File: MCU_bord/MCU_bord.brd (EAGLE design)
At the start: 100 x 80 mm, 1 part

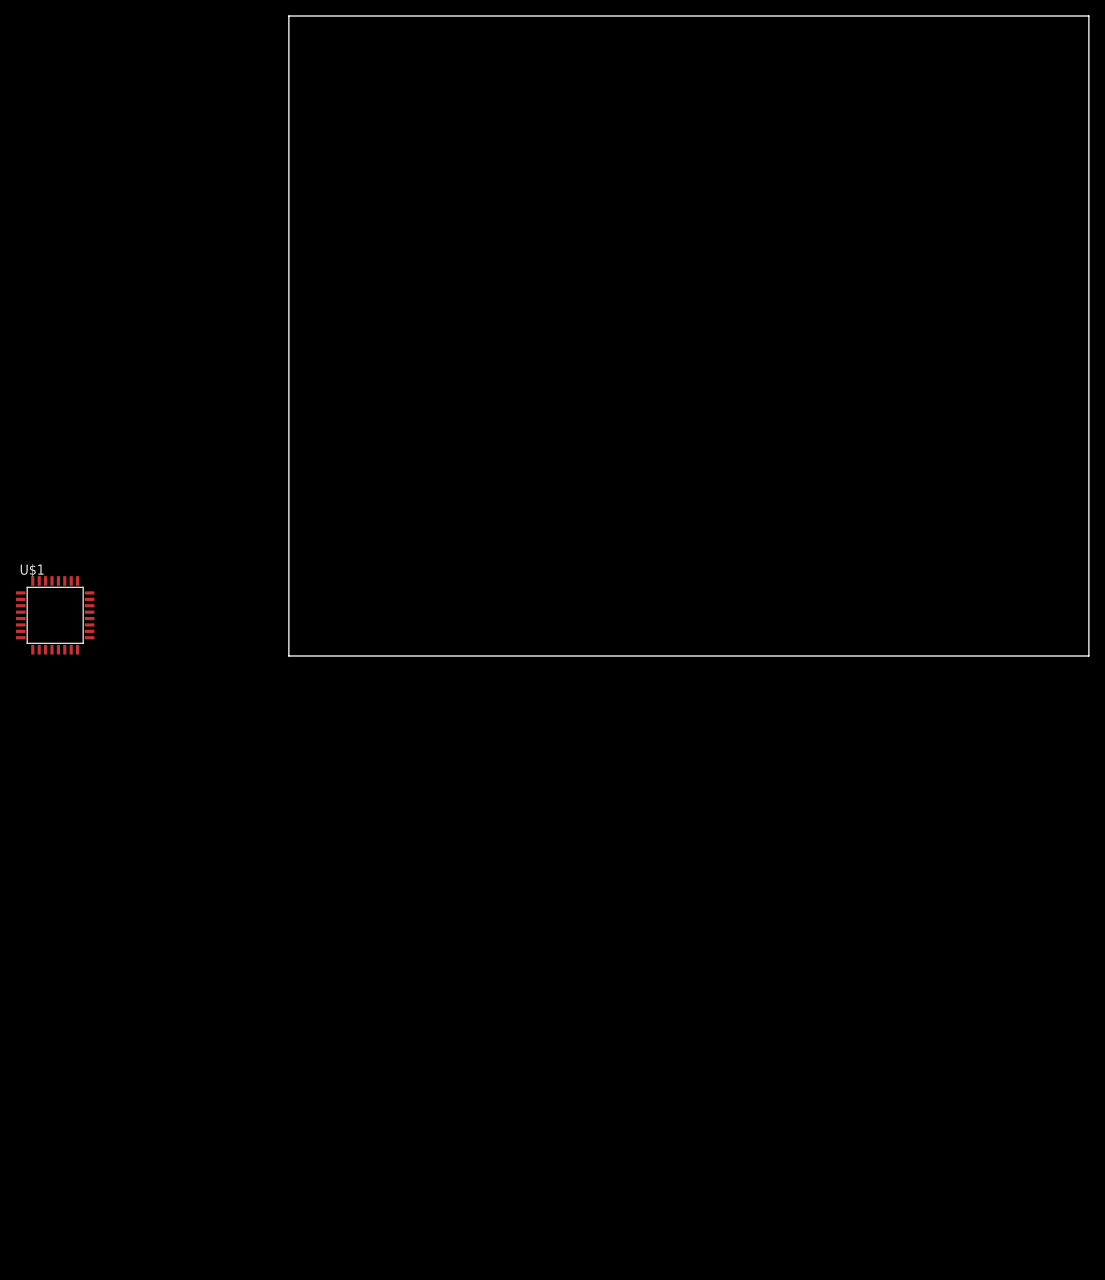
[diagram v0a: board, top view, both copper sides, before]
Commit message: mcu側に着手
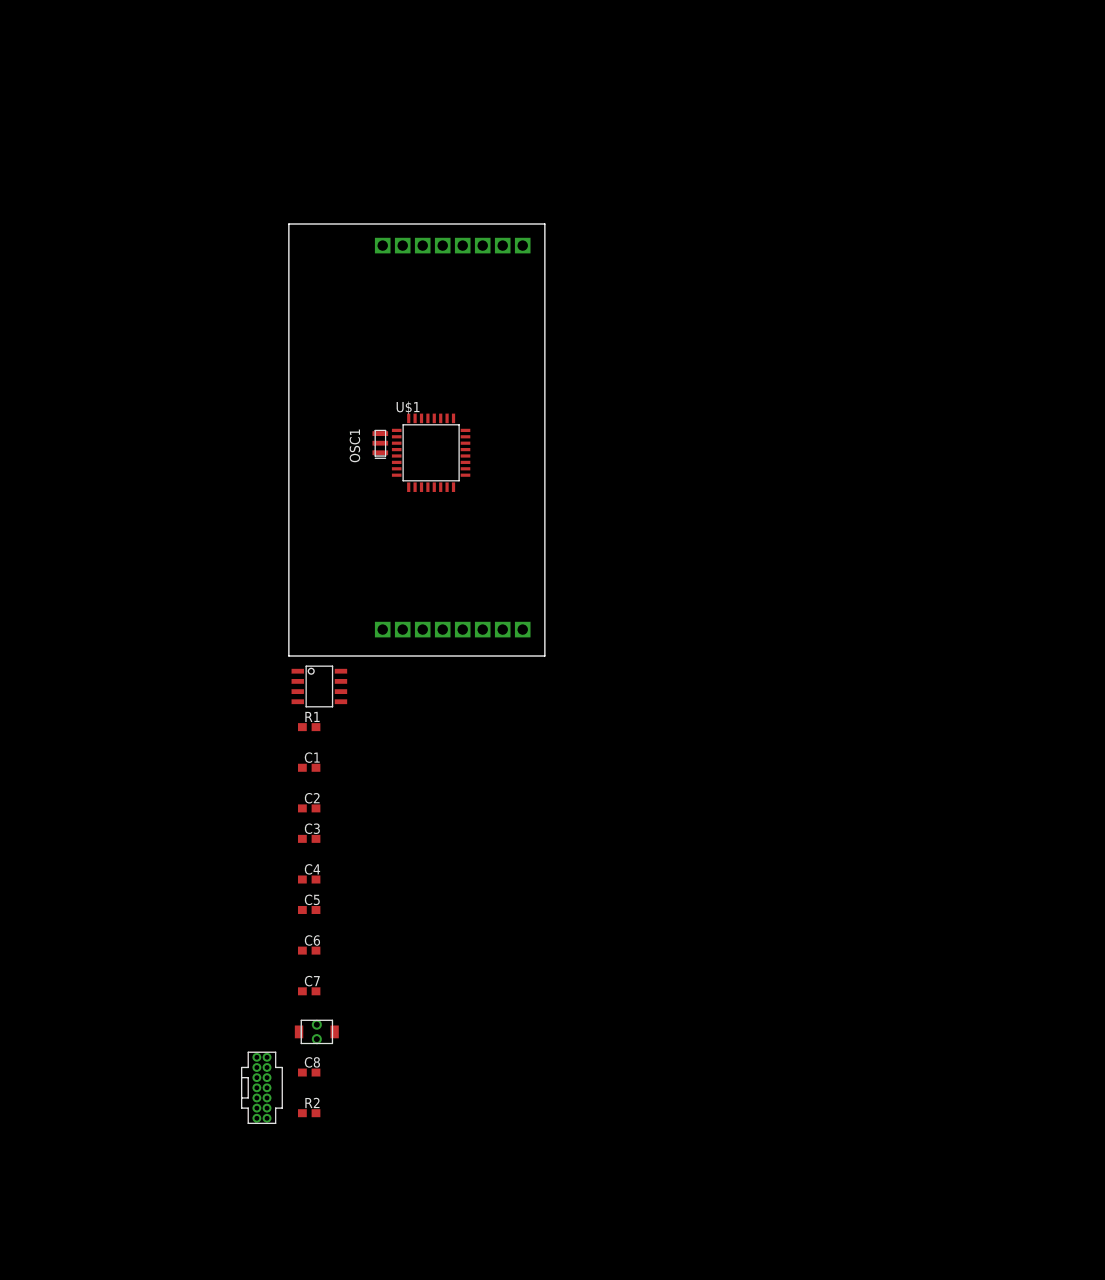
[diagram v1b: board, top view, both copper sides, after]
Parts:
- added C1, C4, C8: 0.1u, rcl:C1608
- added C2, C3, C7: 10u, rcl:C1608
- added C5: 4.7u, rcl:C1608
- added C6: 1u, rcl:C1608
- added CON1, CON2: (no value), user_conector:JQ_S8P
- added IC1: (no value), user_ic:SOIC8
- added OSC1: 12M, user_osc:CSTNE#
- added R1, R2: 10k, user_rcl:1608
- added U$2: TAKUTOSUITTI2, user_swich:TAKUTOSUITTI2
- added U$3: BOX14P, user_conector:CON_HEDA14P_1.27
- moved U$1 51.2 mm to (17.8, 25.4)
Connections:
- new net +3V3: C2.1, C4.2, C5.1, CON1.P$6, IC1.P$5, U$1.1, U$1.17
- new net +5V: C1.1, C3.1, CON1.P$5, IC1.P$3, R1.1
- new net CAN_N: CON2.P$8, IC1.P$6
- new net CAN_P: CON2.P$7, IC1.P$7
- new net CAN_RX: IC1.P$4, U$1.21
- new net CAN_TX: IC1.P$1, U$1.22
- new net COAST: CON1.P$3
- new net DIR: CON1.P$4
- new net FF1: CON1.P$2
- new net FF2: CON1.P$1
- new net GND: C1.2, C2.2, C3.2, C4.1, C5.2, C6.2, C7.2, C8.2, CON1.P$7, CON1.P$8, CON2.P$1, CON2.P$3, IC1.P$2, OSC1.P$2, R2.2, U$1.16, U$1.32, U$2.P$1, U$3.11, U$3.5, U$3.7
- new net N$1: OSC1.P$1, U$1.3
- new net N$2: OSC1.P$3, U$1.2
- new net N$3: R2.1, U$1.31
- new net N$7: IC1.P$8, R1.2
- new net NRST: U$1.4, U$3.12
- new net PWM: CON2.P$5
- new net RESET: CON2.P$6
- new net T_JCLK/SWCLK: U$1.24, U$3.6
- new net T_JTDI: U$1.25, U$3.10
- new net T_JTDO/SWO: U$1.26, U$3.8
- new net T_JTMS/SWDIO: U$1.23, U$3.4
- new net T_VCC: U$3.3
- new net T_VCP_RX: U$1.30, U$3.13
- new net T_VCP_TX: U$1.29, U$3.14
- new net VDDA: C6.1, C7.1, C8.1, CON2.P$4, U$1.5, U$2.P$2
- new net VIOUT: CON2.P$2
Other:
- board size 100 x 80 mm -> 32 x 54 mm

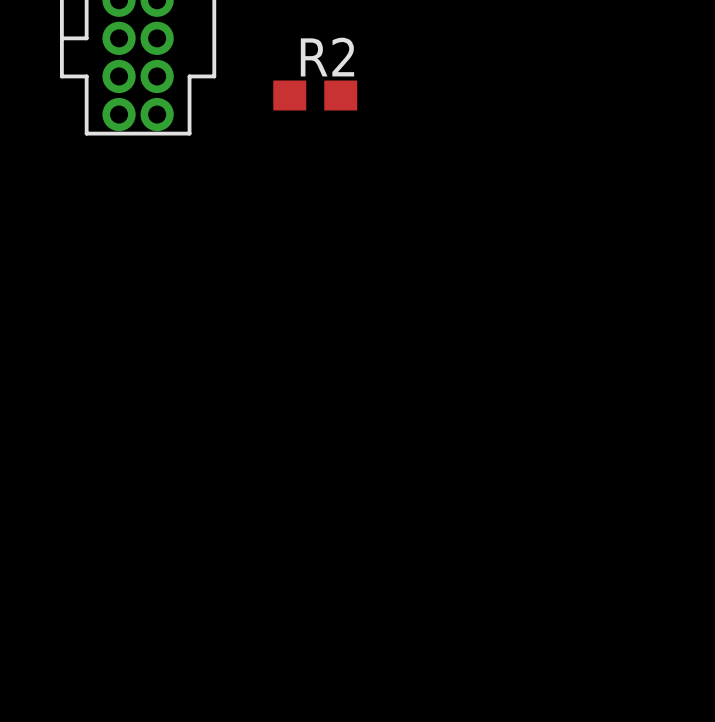
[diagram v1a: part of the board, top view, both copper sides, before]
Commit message: mcu側回路図多分完成。基板側に着手する予定
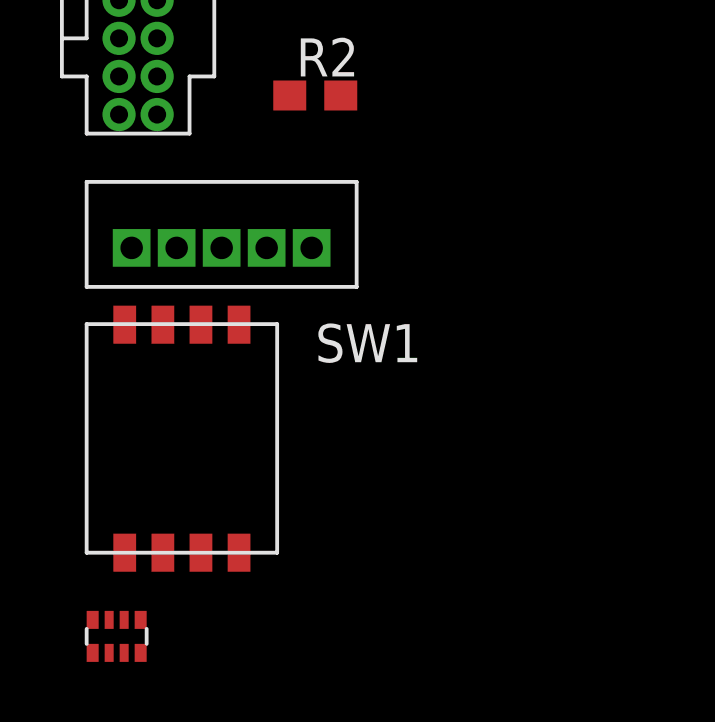
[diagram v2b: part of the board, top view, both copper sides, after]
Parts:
- added R_I1: (no value), user_rcl:1005X4RESISTOR
- added SW1: (no value), user_swich:DIPSW4
- added U$4: ZH_5P, user_conector:ZH_5P
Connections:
- new net A_CH: U$1.20, U$4.PIN3
- new net B_CH: U$1.19, U$4.PIN1
- new net ID1: R_I1.1, SW1.P$8, U$1.15
- new net ID2: R_I1.2, SW1.P$7, U$1.18
- new net ID3: R_I1.3, SW1.P$6, U$1.27
- new net ID4: R_I1.4, SW1.P$5, U$1.28
- net +3V3: now also R_I1.5, R_I1.6, R_I1.7, R_I1.8
- net +5V: now also U$4.PIN2
- net COAST: now also U$1.7
- net DIR: now also U$1.6
- net FF1: now also U$1.8
- net FF2: now also U$1.9
- net GND: now also SW1.P$1, SW1.P$2, SW1.P$3, SW1.P$4, U$4.PIN5
- net PWM: now also U$1.14
- net RESET: now also U$1.13
- net VIOUT: now also U$1.11
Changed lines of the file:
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@@
 </element>
 <element name="U$3" library="user_conector" package="CON_HEDA14P_1.27" value="BOX14P" x="-5.08" y="-58.42" smashed="yes"/>
+<element name="U$4" library="user_conector" package="ZH_5P" value="ZH_5P" x="-5.08" y="-62.23" smashed="yes"/>
+<element name="SW1" library="user_swich" package="DIPSW4" value="" x="-2.54" y="-68.58" smashed="yes">
+<attribute name="NAME" x="2.54" y="-66.04" size="1.27" layer="25"/>
+<attribute name="VALUE" x="2.54" y="-71.12" size="1.27" layer="27"/>
+</element>
+<element name="R_I1" library="user_rcl" package="1005X4RESISTOR" value="" x="-5.08" y="-74.93" smashed="yes"/>
 </elements>
 <signals>
@@
 <signal name="FF2">
 <contactref element="CON1" pad="P$1"/>
+<contactref element="U$1" pad="9"/>
+<wire x1="14.98" y1="21.1" x2="11.73" y2="51.3" width="0" layer="19" extent="1-1"/>
 </signal>
 <signal name="FF1">
 <contactref element="CON1" pad="P$2"/>
+<contactref element="U$1" pad="8"/>
+<wire x1="13.48" y1="22.6" x2="14.23" y2="51.3" width="0" layer="19" extent="1-1"/>
 </signal>
 <signal name="COAST">
 <contactref element="CON1" pad="P$3"/>
+<contactref element="U$1" pad="7"/>
+<wire x1="13.48" y1="23.4" x2="16.73" y2="51.3" width="0" layer="19" extent="1-1"/>
 </signal>
 <signal name="DIR">
 <contactref element="CON1" pad="P$4"/>
+<contactref element="U$1" pad="6"/>
+<wire x1="13.48" y1="24.2" x2="19.23" y2="51.3" width="0" layer="19" extent="1-1"/>
 </signal>
 <signal name="VIOUT">
 <contactref element="CON2" pad="P$2"/>
+<contactref element="U$1" pad="11"/>
+<wire x1="14.23" y1="3.3" x2="16.58" y2="21.1" width="0" layer="19" extent="1-1"/>
 </signal>
 <signal name="VDDA">
@@
 <signal name="PWM">
 <contactref element="CON2" pad="P$5"/>
+<contactref element="U$1" pad="14"/>
+<wire x1="21.73" y1="3.3" x2="18.98" y2="21.1" width="0" layer="19" extent="1-1"/>
 </signal>
 <signal name="RESET">
 <contactref element="CON2" pad="P$6"/>
+<contactref element="U$1" pad="13"/>
+<wire x1="24.23" y1="3.3" x2="18.18" y2="21.1" width="0" layer="19" extent="1-1"/>
 </signal>
 <signal name="CAN_P">
@@
 <contactref element="U$3" pad="7"/>
 <contactref element="U$3" pad="5"/>
+<contactref element="U$4" pad="PIN5"/>
+<contactref element="SW1" pad="P$1"/>
+<contactref element="SW1" pad="P$4"/>
+<contactref element="SW1" pad="P$3"/>
+<contactref element="SW1" pad="P$2"/>
 <wire x1="26.73" y1="51.3" x2="29.23" y2="51.3" width="0" layer="19" extent="1-1"/>
 <wire x1="14.98" y1="29.7" x2="26.73" y2="51.3" width="0" layer="19" extent="1-1"/>
@@
 <wire x1="3.39" y1="-52.07" x2="1.27" y2="-46.99" width="0" layer="19" extent="1-1"/>
 <wire x1="3.39" y1="-57.15" x2="3.39" y2="-52.07" width="0" layer="19" extent="1-1"/>
+<wire x1="2.42" y1="-62.23" x2="3.39" y2="-57.15" width="0" layer="19" extent="1-1"/>
 <wire x1="-4" y1="-56.515" x2="3.39" y2="-57.15" width="0" layer="19" extent="1-1"/>
 <wire x1="-4" y1="-53.975" x2="-4" y2="-56.515" width="0" layer="19" extent="1-1"/>
 <wire x1="-4" y1="-52.705" x2="-4" y2="-53.975" width="0" layer="19" extent="1-1"/>
+<wire x1="0" y1="-72.39" x2="2.42" y2="-62.23" width="0" layer="19" extent="1-1"/>
+<wire x1="-1.27" y1="-72.39" x2="0" y2="-72.39" width="0" layer="19" extent="1-1"/>
+<wire x1="-2.54" y1="-72.39" x2="-1.27" y2="-72.39" width="0" layer="19" extent="1-1"/>
+<wire x1="-3.81" y1="-72.39" x2="-2.54" y2="-72.39" width="0" layer="19" extent="1-1"/>
 </signal>
 <signal name="+5V">
@@
 <contactref element="C1" pad="1"/>
 <contactref element="C3" pad="1"/>
+<contactref element="U$4" pad="PIN2"/>
 <wire x1="1.11" y1="-4.445" x2="21.73" y2="51.3" width="0" layer="19" extent="1-1"/>
 <wire x1="1.69" y1="-8.89" x2="1.11" y2="-4.445" width="0" layer="19" extent="1-1"/>
 <wire x1="1.69" y1="-13.97" x2="1.69" y2="-8.89" width="0" layer="19" extent="1-1"/>
 <wire x1="1.69" y1="-22.86" x2="1.69" y2="-13.97" width="0" layer="19" extent="1-1"/>
+<wire x1="-2.08" y1="-62.23" x2="1.69" y2="-22.86" width="0" layer="19" extent="1-1"/>
 </signal>
 <signal name="+3V3">
@@
 <contactref element="C4" pad="2"/>
 <contactref element="C5" pad="1"/>
-<wire x1="13.48" y1="28.2" x2="24.23" y2="51.3" width="0" layer="19" extent="1-1"/>
-<wire x1="22.08" y1="22.6" x2="13.48" y2="28.2" width="0" layer="19" extent="1-1"/>
-<wire x1="6.51" y1="-5.715" x2="22.08" y2="22.6" width="0" layer="19" extent="1-1"/>
-<wire x1="1.69" y1="-19.05" x2="6.51" y2="-5.715" width="0" layer="19" extent="1-1"/>
-<wire x1="3.39" y1="-27.94" x2="1.69" y2="-19.05" width="0" layer="19" extent="1-1"/>
-<wire x1="1.69" y1="-31.75" x2="3.39" y2="-27.94" width="0" layer="19" extent="1-1"/>
+<contactref element="R_I1" pad="8"/>
+<contactref element="R_I1" pad="5"/>
+<contactref element="R_I1" pad="7"/>
+<contactref element="R_I1" pad="6"/>
+<wire x1="-4.33" y1="-74.63" x2="-4.88" y2="-74.63" width="0" layer="19" extent="1-1"/>
+<wire x1="-3.83" y1="-74.63" x2="-4.33" y2="-74.63" width="0" layer="19" extent="1-1"/>
+<wire x1="-3.28" y1="-74.63" x2="-3.83" y2="-74.63" width="0" layer="19" extent="1-1"/>
+<wire x1="1.69" y1="-31.75" x2="-3.28" y2="-74.63" width="0" layer="19" extent="1-1"/>
+<wire x1="3.39" y1="-27.94" x2="1.69" y2="-31.75" width="0" layer="19" extent="1-1"/>
+<wire x1="1.69" y1="-19.05" x2="3.39" y2="-27.94" width="0" layer="19" extent="1-1"/>
+<wire x1="6.51" y1="-5.715" x2="1.69" y2="-19.05" width="0" layer="19" extent="1-1"/>
+<wire x1="22.08" y1="22.6" x2="6.51" y2="-5.715" width="0" layer="19" extent="1-1"/>
+<wire x1="13.48" y1="28.2" x2="22.08" y2="22.6" width="0" layer="19" extent="1-1"/>
+<wire x1="24.23" y1="51.3" x2="13.48" y2="28.2" width="0" layer="19" extent="1-1"/>
 </signal>
 <signal name="N$7">
@@
 <contactref element="U$3" pad="3"/>
 </signal>
+<signal name="B_CH">
+<contactref element="U$4" pad="PIN1"/>
+<contactref element="U$1" pad="19"/>
+<wire x1="22.08" y1="24.2" x2="-3.58" y2="-62.23" width="0" layer="19" extent="1-1"/>
+</signal>
+<signal name="A_CH">
+<contactref element="U$4" pad="PIN3"/>
+<contactref element="U$1" pad="20"/>
+<wire x1="22.08" y1="25" x2="-0.58" y2="-62.23" width="0" layer="19" extent="1-1"/>
+</signal>
+<signal name="ID1">
+<contactref element="U$1" pad="15"/>
+<contactref element="R_I1" pad="1"/>
+<contactref element="SW1" pad="P$8"/>
+<wire x1="-3.81" y1="-64.79" x2="-4.88" y2="-75.73" width="0" layer="19" extent="1-1"/>
+<wire x1="19.78" y1="21.1" x2="-3.81" y2="-64.79" width="0" layer="19" extent="1-1"/>
+</signal>
+<signal name="ID2">
+<contactref element="U$1" pad="18"/>
+<contactref element="R_I1" pad="2"/>
+<contactref element="SW1" pad="P$7"/>
+<wire x1="-2.54" y1="-64.79" x2="-4.33" y2="-75.73" width="0" layer="19" extent="1-1"/>
+<wire x1="22.08" y1="23.4" x2="-2.54" y2="-64.79" width="0" layer="19" extent="1-1"/>
+</signal>
+<signal name="ID3">
+<contactref element="U$1" pad="27"/>
+<contactref element="R_I1" pad="3"/>
+<contactref element="SW1" pad="P$6"/>
+<wire x1="-1.27" y1="-64.79" x2="-3.83" y2="-75.73" width="0" layer="19" extent="1-1"/>
+<wire x1="18.98" y1="29.7" x2="-1.27" y2="-64.79" width="0" layer="19" extent="1-1"/>
+</signal>
+<signal name="ID4">
+<contactref element="U$1" pad="28"/>
+<contactref element="R_I1" pad="4"/>
+<contactref element="SW1" pad="P$5"/>
+<wire x1="0" y1="-64.79" x2="-3.28" y2="-75.73" width="0" layer="19" extent="1-1"/>
+<wire x1="18.18" y1="29.7" x2="0" y2="-64.79" width="0" layer="19" extent="1-1"/>
+</signal>
 </signals>

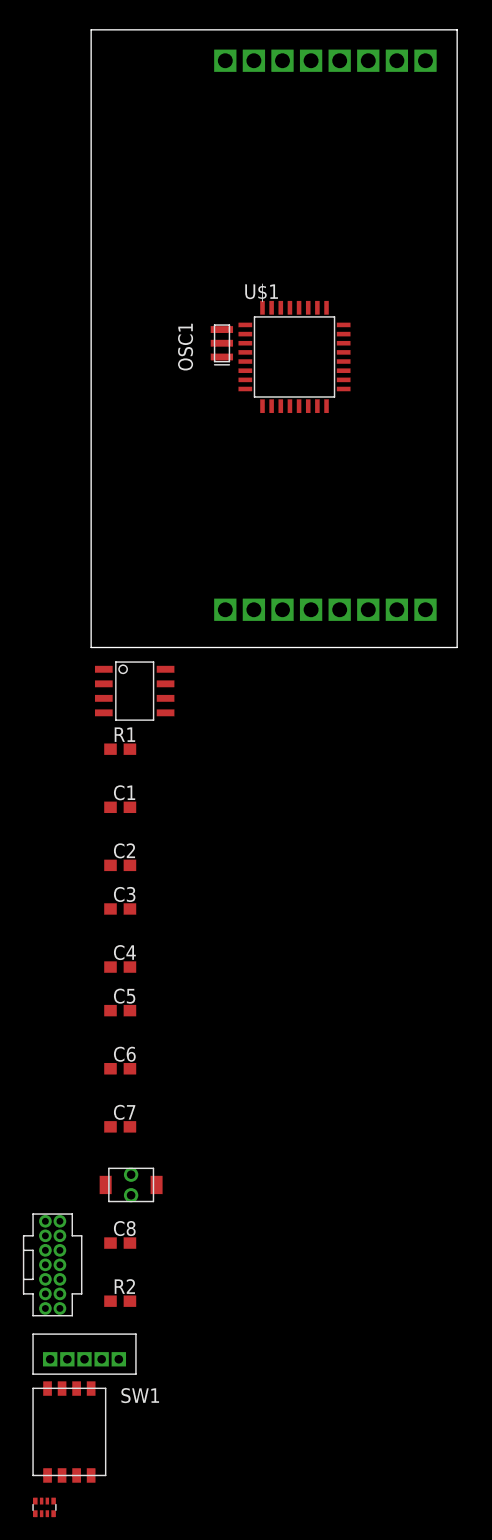
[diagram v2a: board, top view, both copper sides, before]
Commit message: MCU側完成。文字の位置とかの調整をやれば発注できる
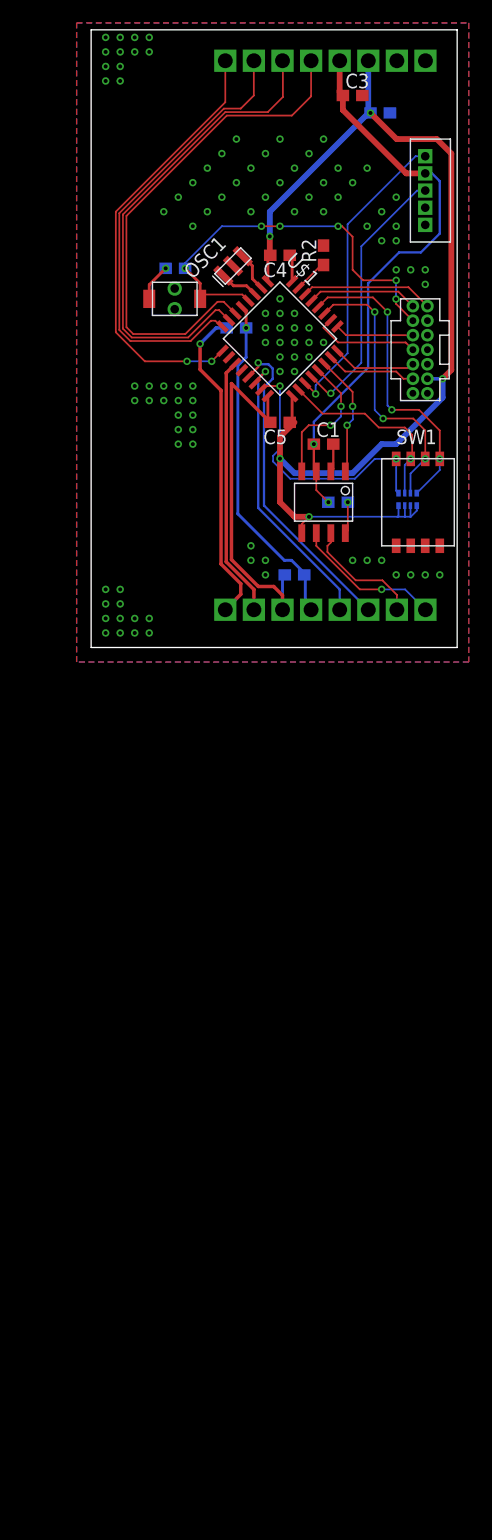
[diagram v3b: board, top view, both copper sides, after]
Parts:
- moved U$4 112.1 mm to (29.2, 44.5), turned to 270 degrees
- moved U$3 95.7 mm to (30.5, 30.5), turned to 180 degrees
- moved R_I1 93.2 mm to (26.7, 12.7), flipped to the bottom, turned to 180 degrees
- moved R2 93.2 mm to (20.3, 34.3), turned to 90 degrees
- moved SW1 86.8 mm to (27.9, 12.7)
- moved C8 85.4 mm to (7.37, 33.1), flipped to the bottom
- moved U$2 77.6 mm to (5.08, 30.5)
- moved C3 74.0 mm to (22.9, 48.3)
- moved C2 69.6 mm to (25.3, 46.7), flipped to the bottom, turned to 180 degrees
- moved C6 65.6 mm to (12.7, 27.9), flipped to the bottom
- moved C4 63.8 mm to (16.5, 34.3), turned to 180 degrees
- moved C5 53.3 mm to (16.5, 19.7), turned to 180 degrees
- moved C7 50.6 mm to (17.8, 6.35), flipped to the bottom
- moved C1 36.4 mm to (20.3, 17.8)
- moved R1 28.8 mm to (21.6, 12.7), flipped to the bottom, turned to 180 degrees
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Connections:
- removed net T_VCC: U$3.3
- net +3V3: now also U$3.3
- net NRST: now also C8.1, U$2.P$2
- net VDDA: no longer C8.1, U$2.P$2
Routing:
- net +3V3: track 0.00 -> 100.4 mm, vias 0 -> 5
- net GND: track 0.00 -> 69.0 mm, vias 0 -> 108
- net +5V: track 0.00 -> 49.9 mm, vias 0 -> 2
- net DIR: track 0.00 -> 44.7 mm
- net COAST: track 0.00 -> 42.3 mm
- net FF1: track 0.00 -> 39.6 mm
- net FF2: track 0.00 -> 38.5 mm, vias 0 -> 2
- net NRST: track 0.00 -> 35.9 mm, vias 0 -> 6
- net VDDA: track 0.00 -> 29.9 mm, vias 0 -> 1
- net RESET: track 0.00 -> 28.2 mm, vias 0 -> 1
- net ID4: track 0.00 -> 26.9 mm, vias 0 -> 3
- net B_CH: track 0.00 -> 26.6 mm, vias 0 -> 1
- net PWM: track 0.00 -> 25.4 mm, vias 0 -> 1
- net ID3: track 0.00 -> 24.7 mm, vias 0 -> 3
- net A_CH: track 0.00 -> 24.0 mm, vias 0 -> 1
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- added copper zone on layer 1, net GND
- added copper zone on layer 16, net GND
